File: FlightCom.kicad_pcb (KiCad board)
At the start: 4 copper layers, 86.5 x 57.5 mm, 149 parts, among them IC1 SN74HCT125DR, J1 Molex Microfit, J10 Conn_01x03_Socket, J11 Conn_01x02_Socket, J2 Conn_02x03_Counter_Clockwise, J7 Conn_01x02_Socket, J8 Conn_01x02_Socket, Q1 SI7232DN-T1-GE3, Q4 SI7232DN-T1-GE3, U1 TPS62153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

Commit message: update
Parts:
- H1, H2, H3, H4: footprint MountingHole:MountingHole_2.2mm_M2 -> MountingHole:MountingHole_3.2mm_M3
- moved C1 26.4 mm to (146.0, 90.7)
- moved C9 20.7 mm to (141.0, 79.7), turned to 180 degrees
- moved C15 20.4 mm to (124.2, 98.2), turned to 180 degrees
- moved C7 9.58 mm to (122.4, 84.9)
- moved C5 7.45 mm to (122.4, 82.8), turned to -90 degrees
- moved H1 2.37 mm to (96.3, 110.6)
- moved C30 1.78 mm to (133.8, 106.8)
- moved H2 1.64 mm to (95.9, 62.4)
- moved H4 1.20 mm to (174.6, 110.8)
- moved H3 1.12 mm to (174.1, 62.4)
- moved J11 1.10 mm to (162.2, 61.2)
- moved C17 0.88 mm to (125.1, 77.2), turned to 180 degrees
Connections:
- C29 pad 2: Net-(U7-VS) -> +3.3V
- C30 pad 1: Net-(U7-VDDI/O) -> +3.3V
- C32 pad 2: Net-(U7-VS) -> +3.3V
- Q1 pad 9: (no net) -> Net-(J11-Pin_1)
- U6 pad 13: BMI088_GYRO_INT -> unconnected-(U6-INT4-Pad13)
- U7 pad 1: Net-(U7-VDDI/O) -> +3.3V
- U7 pad 6: Net-(U7-VS) -> +3.3V
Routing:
- net Net-(U7-VS): track 3.45 -> 0.00 mm
- net Net-(U7-VDDI/O): track 3.35 -> 0.00 mm
- net VBAT-: track 202.1 -> 199.0 mm, vias 107 -> 108
- net +3.3V: track 178.7 -> 181.0 mm, vias 53 -> 57
- net ADXL375_SCLK: track 25.2 -> 24.5 mm
- net HSE_IN: track 10.4 -> 10.9 mm
- net Net-(J7-Pin_1): track 8.04 -> 8.57 mm
- net BMI088_GYRO_INT: track 14.8 -> 14.3 mm
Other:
- board size 86.5 x 57.5 mm -> 87.3 x 57.5 mm

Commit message: reroute
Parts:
- removed C16, C27: 100nF, Capacitor_SMD:C_0402_1005Metric
- removed C24, C25: 10uF, Capacitor_SMD:C_0402_1005Metric_Pad0.74x0.62mm_HandSolder
- removed R23, R24, R25, R26, R27, R28, R29, R30, R31: 10K, Resistor_SMD:R_0402_1005Metric
- removed R32: 4.7K, Resistor_SMD:R_0402_1005Metric
- removed Rechargeable1: 3.1V Battery, Battery:BatteryHolder_Seiko_MS621F
- removed U14: KLM8G1GETF-B041, EMMC:KLMBG2JENB-B041_SAM
- removed X1: 1XXD32000MBA, EasyEDA:OSC-SMD_4P-L2.0-W1.6-BL_1XXD
- added BT1: 3098, Battery3V_holder:BAT_3098, F.Cu at (107.0, 105.2)
- added J9: BMI-S-209-F, Lora_shield:LAIRD_BMI-S-209-F, F.Cu at (116.2, 64.0)
- added R34: 10K, Resistor_SMD:R_0402_1005Metric, F.Cu at (146.5, 86.7)
- added R40: 10K, Resistor_SMD:R_0402_1005Metric, F.Cu at (142.6, 74.7)
- added R41: 10K, Resistor_SMD:R_0402_1005Metric, F.Cu at (140.4, 78.3)
- added R42: 10K, Resistor_SMD:R_0402_1005Metric, F.Cu at (142.4, 78.3)
- added R43: 10K, Resistor_SMD:R_0402_1005Metric, F.Cu at (144.3, 78.3)
- added R44: 10K, Resistor_SMD:R_0402_1005Metric, F.Cu at (143.4, 82.5)
- added R45: 10K, Resistor_SMD:R_0402_1005Metric, F.Cu at (143.7, 86.0)
- added U12: THGBMNG5D1LBAIT, EMMC:BGA153N50P14X14_1000X1100X80, F.Cu at (151.3, 77.8)
- added X2: ECS-TXO-32CSMV-320-AN-TR, CLOCK:OSC_ECS-TXO-2520-33-320-AN-TR, F.Cu at (119.5, 86.1)
- C21: value 1nF -> 10uF
- C23: value 10uF -> 10nF
- C3: footprint Capacitor_SMD:C_0402_1005Metric_Pad0.74x0.62mm_HandSolder -> Capacitor_SMD:C_0402_1005Metric
- C39, C41, C42, C43, C44, C45, C46, C48, C49, C50, C51, C52, C53, C54, C55, C56, C58: footprint Capacitor_SMD:C_0201_0603Metric -> Capacitor_SMD:C_0402_1005Metric
- C4: value 10pF -> 0.1µF
- C57: value 36pF -> 39pF; footprint Capacitor_SMD:C_0201_0603Metric -> Capacitor_SMD:C_0402_1005Metric
- D2: footprint EasyEDA:SOD-123_L2.8-W1.8-LS3.7-RD -> zener_diode:SOD3716X135N
- D6, D7: footprint LED_SMD:LED_0805_2012Metric -> LED_SMD:LED_0402_1005Metric
- L2, L4, L5, L6, L7, L8: footprint Inductor_SMD:L_0201_0603Metric -> Inductor_SMD:L_0402_1005Metric
- R12, R9: value 4.7k -> 2.7k
- R16: footprint Resistor_SMD:R_0201_0603Metric -> Resistor_SMD:R_0402_1005Metric
- R3: value 100k -> 10K; footprint Resistor_SMD:R_0402_1005Metric_Pad0.72x0.64mm_HandSolder -> Resistor_SMD:R_0402_1005Metric
- USB1: value C169130 -> 10172013-00011LF; footprint EasyEDA:USB-C-SMD_TYPE-C3.1-02 -> USBC:AMPHENOL_10172013-00011LF
- moved C4 39.8 mm to (157.9, 80.2), turned to -90 degrees
- moved C23 29.8 mm to (122.1, 86.9)
- moved R3 25.1 mm to (145.6, 84.8), turned to 0 degrees
- moved J2 10.4 mm to (149.8, 64.5)
- moved C21 7.69 mm to (152.4, 98.9)
- moved R7 7.25 mm to (148.2, 104.6)
- moved R6 5.97 mm to (154.2, 105.6), turned to 90 degrees
- moved R5 5.22 mm to (150.7, 105.2), turned to -90 degrees
- moved R8 5.19 mm to (148.2, 103.5), turned to 0 degrees
- moved J11 5.14 mm to (165.0, 56.9), turned to 180 degrees
- moved JP1 4.41 mm to (102.4, 63.0)
- moved H2 4.35 mm to (96.0, 58.0)
- moved H3 4.35 mm to (174.0, 58.0)
- moved C48 4.31 mm to (105.0, 63.3)
- moved L2 3.93 mm to (106.5, 62.9)
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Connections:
- C21 pad 1: Net-(USB1-EH) -> VBAT-
- C21 pad 2: VBAT- -> VBUS
- C23 pad 1: VBUS -> HSE_IN
- C23 pad 2: VBAT- -> Net-(X2-OUTPUT)
- C4 pad 2: HSE_IN -> Net-(U12-NC__30)
- R3 pad 1: HSE_IN -> +3.3V
- R3 pad 2: VBAT- -> EMMC_DAT7
- R5 pad 1: Net-(USB1-CC2) -> VBAT-
- R5 pad 2: VBAT- -> Net-(USB1-CC1)
- R6 pad 1: Net-(USB1-CC1) -> Net-(USB1-CC2)
- U11 pad 12: SX1262_DIO2 -> ANT_SW
- U5 pad 39: unconnected-(U5-PE8-Pad39) -> BCD
- U6 pad 1: BMI088_ACCEL_INT -> unconnected-(U6-INT2-Pad1)
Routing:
- net ANT_SW: track 0.00 -> 35.2 mm, vias 0 -> 2
- net +3.3V: track 181.0 -> 154.5 mm
- net Net-(USB1-EH): track 24.4 -> 0.00 mm
- net VBUS: track 28.1 -> 7.51 mm, vias 9 -> 4
- net BCD: track 2.36 -> 21.6 mm, vias 0 -> 2
- net EMMC_CMD: track 45.0 -> 26.6 mm
- net EMMC_DAT6: track 35.2 -> 18.0 mm, vias 2 -> 4
- net COMPANION_TX: track 32.1 -> 47.0 mm, vias 1 -> 2
- net VBAT+: track 60.2 -> 45.6 mm, vias 7 -> 5
- net EMMC_DAT7: track 29.7 -> 15.3 mm, vias 2 -> 3
- net Backup: track 35.5 -> 49.0 mm
- net SX1262_DIO2: track 13.2 -> 0.00 mm, vias 2 -> 0
- net Net-(U12-NC__30): track 0.00 -> 10.5 mm, vias 0 -> 2
- net nRST: track 30.2 -> 40.5 mm, vias 2 -> 3
- net SWDIO: track 16.7 -> 26.5 mm
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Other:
- board size 87.3 x 57.5 mm -> 87.3 x 62.2 mm
- board text added: "FLIGHT COMPUTER"

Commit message: rm led
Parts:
- removed D5, D7: LED, LED_SMD:LED_0402_1005Metric
- removed R16: 100R, Resistor_SMD:R_0402_1005Metric
- removed R18: 1k, Resistor_SMD:R_0402_1005Metric
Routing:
- net +3.3V: track 154.5 -> 145.7 mm, vias 57 -> 55
- net Net-(D7-A): track 2.16 -> 0.00 mm
- net Net-(D5-A): track 1.01 -> 0.00 mm

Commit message: run checked
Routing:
- net VBAT-: track 208.0 -> 210.1 mm, vias 114 -> 112
- net BMI088_ACCEL_INT: track 27.0 -> 25.7 mm
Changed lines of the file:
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@@
 	)
 	(segment
+		(start 123.4 90.8)
+		(end 123.4 91.05)
+		(width 0.3)
+		(layer "F.Cu")
+		(net 2)
+	)
+	(segment
 		(start 151.6 76.55)
 		(end 151.6 76.797487)
@@
 	)
 	(segment
-		(start 123.2325 78.4)
-		(end 123.25 78.4175)
-		(width 0.5)
-		(layer "F.Cu")
-		(net 2)
-	)
-	(segment
 		(start 104.8 64.45)
 		(end 103.055 64.45)
@@
 	)
 	(segment
-		(start 123.25 78.4)
-		(end 122 78.4)
-		(width 0.3)
-		(layer "F.Cu")
-		(net 2)
-	)
-	(segment
 		(start 110.04 78.21)
 		(end 109.675 78.21)
@@
 	)
 	(segment
+		(start 123.25 79.65)
+		(end 122 78.4)
+		(width 0.3)
+		(layer "F.Cu")
+		(net 2)
+	)
+	(segment
 		(start 146 90.1325)
 		(end 146.2075 90.1325)
@@
 	)
 	(segment
+		(start 123.15 90.55)
+		(end 123.4 90.8)
+		(width 0.3)
+		(layer "F.Cu")
+		(net 2)
+	)
+	(segment
+		(start 123.4 91.05)
+		(end 124.4 91.05)
+		(width 0.3)
+		(layer "F.Cu")
+		(net 2)
+	)
+	(segment
 		(start 137.725 96.6)
 		(end 137.725 97.375)
@@
 	)
 	(segment
+		(start 124.4 90.55)
+		(end 123.15 90.55)
+		(width 0.3)
+		(layer "F.Cu")
+		(net 2)
+	)
+	(segment
 		(start 164.35 79.15)
 		(end 164.3 79.15)
@@
 	)
 	(via
-		(at 124.4 91.05)
-		(size 0.4)
-		(drill 0.2)
-		(layers "F.Cu" "B.Cu")
-		(net 2)
-	)
-	(via
 		(at 120.25 75.05)
 		(size 0.6)
@@
 	)
 	(via
-		(at 123.25 79.65)
-		(size 0.6)
-		(drill 0.3)
-		(layers "F.Cu" "B.Cu")
-		(net 2)
-	)
-	(via
 		(at 158.3 95.75)
 		(size 0.6)
@@
 	)
 	(via
-		(at 123.25 78.4)
+		(at 123.25 79.65)
 		(size 0.6)
 		(drill 0.3)
@@
 	)
 	(via
-		(at 124.4 90.55)
+		(at 123.15 90.55)
 		(size 0.4)
 		(drill 0.2)
@@
 	)
 	(segment
-		(start 124.4 90.55)
-		(end 124.4 91.05)
-		(width 0.3)
-		(layer "In1.Cu")
-		(net 2)
-	)
-	(segment
 		(start 100.025 83.575)
 		(end 100.025 84.225)
@@
 	)
 	(segment
-		(start 124.4 90.55)
-		(end 122.15 90.55)
+		(start 148.0575 94.4825)
+		(end 148.025 94.45)
 		(width 0.3)
 		(layer "In1.Cu")
@@
 	)
 	(segment
-		(start 148.0575 94.4825)
-		(end 148.025 94.45)
+		(start 123.15 90.55)
+		(end 122.15 90.55)
 		(width 0.3)
 		(layer "In1.Cu")
@@
 	)
 	(segment
-		(start 124.95 81.35)
-		(end 124.95 90)
+		(start 139.169239 82.05)
+		(end 138.25 82.05)
 		(width 0.3)
 		(layer "In1.Cu")
@@
 	)
 	(segment
-		(start 139.169239 82.05)
-		(end 138.25 82.05)
+		(start 124.95 88.75)
+		(end 124.95 81.35)
 		(width 0.3)
 		(layer "In1.Cu")
@@
 	)
 	(segment
-		(start 123.25 79.65)
-		(end 124.95 81.35)
+		(start 122.15 90.55)
+		(end 122.1 90.5)
 		(width 0.3)
 		(layer "In1.Cu")
@@
 	)
 	(segment
-		(start 98.975 88.825)
-		(end 99.125 88.825)
-		(width 0.5)
+		(start 123.15 90.55)
+		(end 124.95 88.75)
+		(width 0.3)
 		(layer "In1.Cu")
 		(net 2)
 	)
 	(segment
-		(start 122.15 90.55)
-		(end 122.1 90.5)
-		(width 0.3)
+		(start 98.975 88.825)
+		(end 99.125 88.825)
+		(width 0.5)
 		(layer "In1.Cu")
 		(net 2)
@@
 	)
 	(segment
+		(start 124.95 81.35)
+		(end 123.25 79.65)
+		(width 0.3)
+		(layer "In1.Cu")
+		(net 2)
+	)
+	(segment
 		(start 101.925 99.325)
 		(end 101.725 99.325)
@@
 	)
 	(segment
-		(start 124.95 90)
-		(end 124.4 90.55)
-		(width 0.3)
-		(layer "In1.Cu")
-		(net 2)
-	)
-	(segment
 		(start 166.15 83.2)
 		(end 166.1 83.15)
@@
 	)
 	(segment
-		(start 126.575 106.45)
-		(end 127.365 106.45)
-		(width 0.2)
-		(layer "F.Cu")
-		(net 117)
-	)
-	(segment
 		(start 123.65 104.65)
 		(end 123.65 108.469239)
@@
 	)
 	(segment
-		(start 127.365 106.45)
-		(end 127.775 106.86)
-		(width 0.2)
+		(start 124.030761 108.85)
+		(end 126.45 108.85)
+		(width 0.3)
 		(layer "F.Cu")
 		(net 117)
 	)
 	(segment
-		(start 124.030761 108.85)
-		(end 126.45 108.85)
-		(width 0.3)
+		(start 127.75 106.835)
+		(end 127.775 106.86)
+		(width 0.2)
 		(layer "F.Cu")
 		(net 117)

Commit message: rearrange
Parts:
- moved C12 25.1 mm to (135.3, 99.0), turned to 180 degrees
- moved C10 22.1 mm to (142.6, 81.4), turned to 90 degrees
- moved C19 21.5 mm to (120.5, 99.5), turned to 90 degrees
- moved FB1 21.4 mm to (119.2, 99.8), turned to 90 degrees
- moved C11 18.9 mm to (117.6, 99.4), turned to -90 degrees
- moved C14 18.9 mm to (116.2, 99.4), turned to -90 degrees
- moved C3 3.72 mm to (119.5, 83.8), turned to 180 degrees
- moved C9 1.80 mm to (141.7, 81.4), turned to 90 degrees
- moved R44 1.00 mm to (144.2, 81.8)
- moved C2 0.49 mm to (121.0, 91.5)
- moved C7 0.39 mm to (122.2, 85.3)
- moved C28 0.25 mm to (136.3, 98.0)
- moved C6 0.16 mm to (122.0, 90.9)
- moved C23 0.15 mm to (122.1, 87.0)
- moved C5 0.08 mm to (122.2, 82.8), turned to 90 degrees
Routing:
- net VBAT-: track 210.1 -> 179.7 mm
- net +3.3V: track 145.7 -> 128.4 mm, vias 55 -> 49
- net +3.3VA: track 24.7 -> 14.3 mm, vias 3 -> 2
- net GNSS_SafeBoot: track 29.3 -> 27.9 mm
- net +5V: vias 6 -> 5

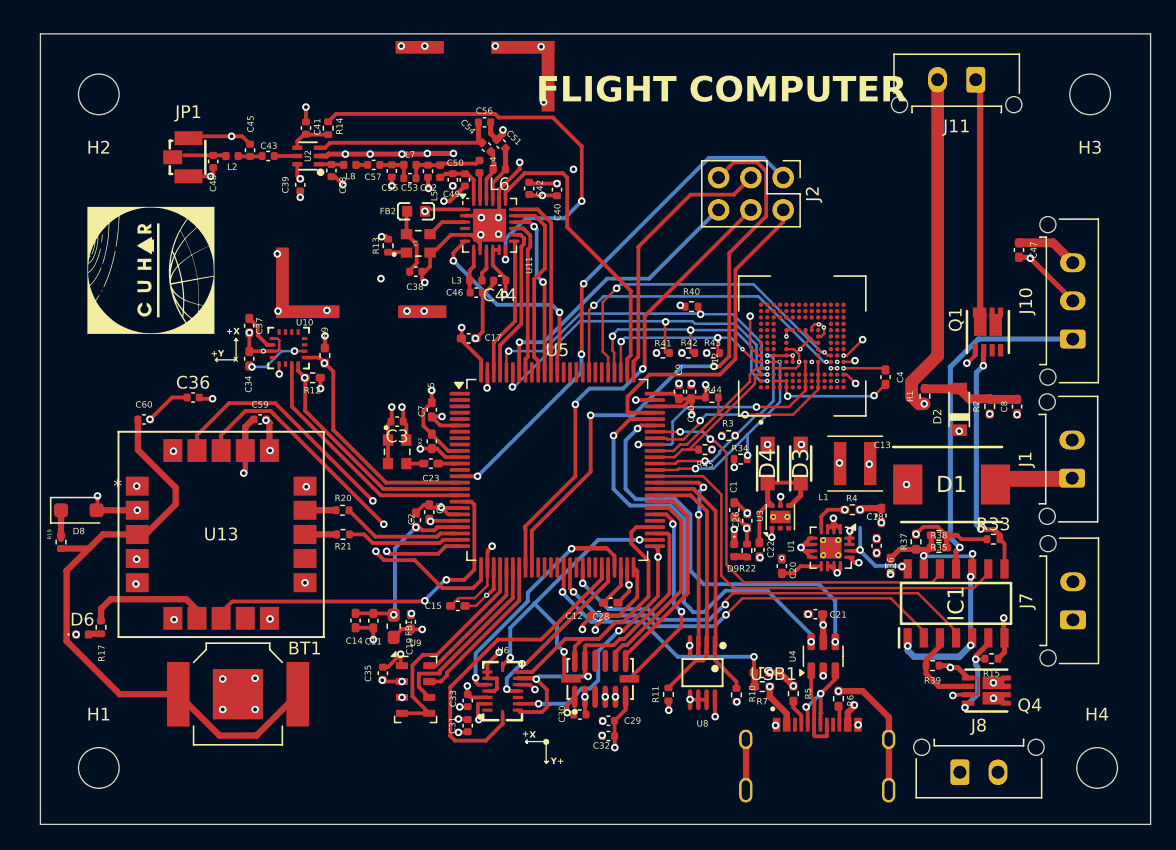
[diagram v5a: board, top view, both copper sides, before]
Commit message: cleanup track and vias
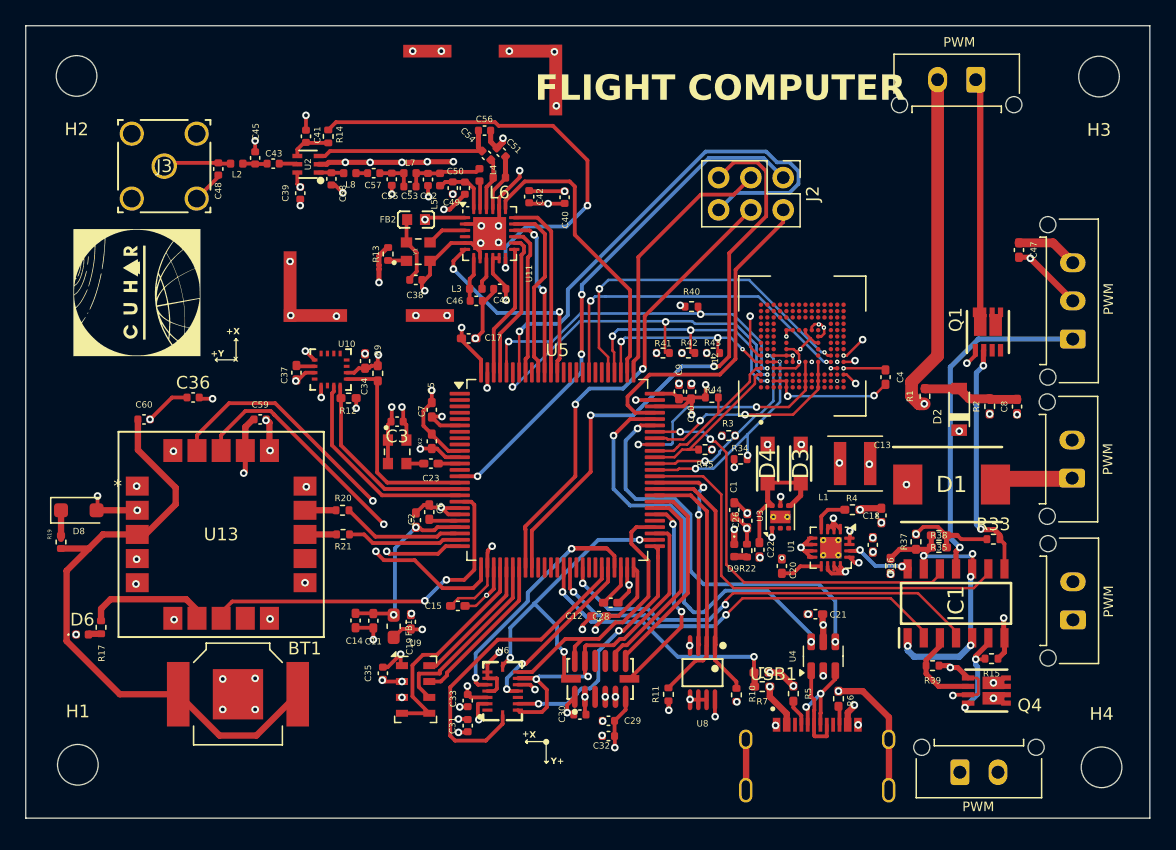
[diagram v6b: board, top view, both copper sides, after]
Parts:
- removed JP1: U.FL-R-SMT-1(10), EasyEDA:ANT-SMD_UFL-R-SMT-1-10
- added J3: RF2-04A-T-00-50-G, SMA_connector:CONN_RF2-04A-T-00-50-G_ADM, F.Cu at (101.1, 63.6)
- moved C34 9.12 mm to (117.0, 79.0)
- moved C37 5.24 mm to (111.5, 79.9)
- moved R9 4.39 mm to (118.0, 80.0)
- moved U10 3.71 mm to (114.2, 79.7)
- moved R12 3.24 mm to (115.7, 81.9)
- moved H2 2.27 mm to (94.2, 56.5)
- moved G*** 2.07 mm to (99.0, 73.6)
- moved H1 1.67 mm to (94.3, 110.8)
- moved H3 1.57 mm to (174.7, 56.6)
- moved C40 0.85 mm to (132.7, 66.1)
- moved C45 0.72 mm to (108.3, 63.0)
- moved C43 0.72 mm to (109.7, 63.5)
- moved C48 0.71 mm to (105.4, 63.9)
- moved L2 0.70 mm to (106.8, 63.5)
- moved J9 0.67 mm to (116.8, 64.3)
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- renumbered J11 to PWM, J10 to PWM, J8 to PWM, J1 to PWM, J7 to PWM
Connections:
- C34 pad 2: Net-(U10-VDD) -> +3.3V
- U10 pad 2: Net-(U10-VDD) -> +3.3V
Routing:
- net BOOT0: track 22.4 -> 41.0 mm
- net VBAT-: track 179.7 -> 172.0 mm
- net +3.3V: track 128.4 -> 133.5 mm, vias 49 -> 46
- net Net-(U10-VDD): track 4.67 -> 0.00 mm, vias 2 -> 0
- net MMC5983MA_SDA: track 18.6 -> 15.5 mm, vias 1 -> 0
- net MMC5983MA_INT: track 19.4 -> 16.4 mm
- net MMC5983MA_SCL: track 19.0 -> 16.6 mm, vias 1 -> 0
- net Net-(C48-Pad2): track 3.19 -> 5.35 mm
- net EMMC_DAT5: track 26.9 -> 28.8 mm
- net +5V: track 26.8 -> 25.0 mm
- net Net-(U10-CAP): track 3.08 -> 1.46 mm
- net VBAT+: track 45.6 -> 46.9 mm
- net EMMC_CLK: track 26.6 -> 27.9 mm
- net BMI088_ACCEL_CS: track 20.9 -> 20.0 mm, vias 3 -> 2
- net SX1262_SCK: track 15.1 -> 14.4 mm
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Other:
- board size 87.3 x 62.2 mm -> 88.4 x 62.4 mm

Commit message: run drc
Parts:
- renumbered PWM to J1, PWM to J10, PWM to J11, PWM to J7, PWM to J8
